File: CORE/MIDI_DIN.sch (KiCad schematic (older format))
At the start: 60 parts, among them J1 Conn_02x08_Odd_Even, J2 USB_C_Receptacle_USB2.0, J3 Conn_01x04, J5 MAB5100S, J6 MAB5100S, J7 Conn_01x06, Q1 BSS84, Q2 BSS84, SW1 SW_SPDT, SW2 SW_Push_DPDT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

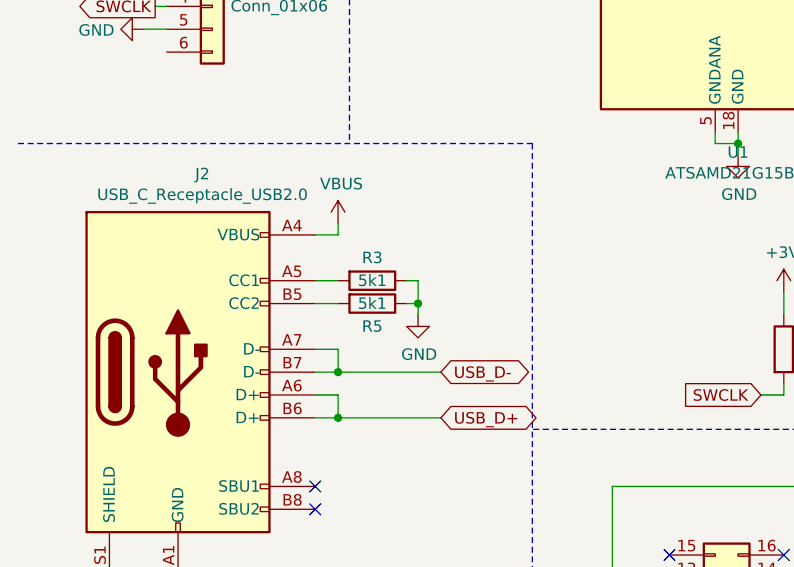
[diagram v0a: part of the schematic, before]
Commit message: Add pulldown for USB power protection
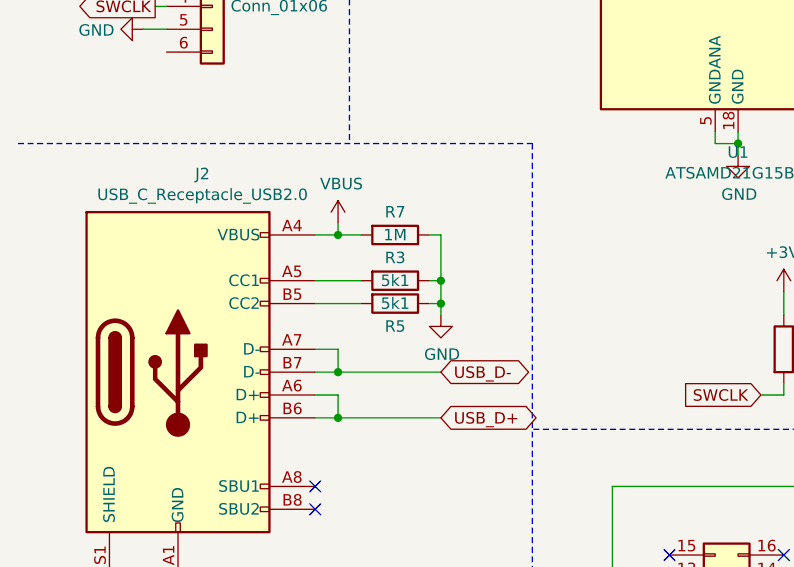
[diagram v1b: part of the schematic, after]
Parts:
- added R7: 1M, Resistor_SMD:R_0603_1608Metric, symbol Device:R
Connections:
- net GND: now also R7.1
- net VBUS: now also R7.2
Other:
- moved on the sheet: R3, R5
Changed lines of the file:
@@
 L Device:R R3
 U 1 1 60B7BED1
-P 2050 5600
-F 0 "R3" V 1950 5600 50  0000 C CNN
-F 1 "5k1" V 2050 5600 50  0000 C CNN
-F 2 "Resistor_SMD:R_0603_1608Metric" V 1980 5600 50  0001 C CNN
-F 3 "~" H 2050 5600 50  0001 C CNN
-	1    2050 5600
+P 2150 5600
+F 0 "R3" V 2050 5600 50  0000 C CNN
+F 1 "5k1" V 2150 5600 50  0000 C CNN
+F 2 "Resistor_SMD:R_0603_1608Metric" V 2080 5600 50  0001 C CNN
+F 3 "~" H 2150 5600 50  0001 C CNN
+	1    2150 5600
 	0    1    1    0
 $EndComp
@@
 L Device:R R5
 U 1 1 60B7CCB7
-P 2050 5700
-F 0 "R5" V 2150 5700 50  0000 C CNN
-F 1 "5k1" V 2050 5700 50  0000 C CNN
-F 2 "Resistor_SMD:R_0603_1608Metric" V 1980 5700 50  0001 C CNN
-F 3 "~" H 2050 5700 50  0001 C CNN
-	1    2050 5700
+P 2150 5700
+F 0 "R5" V 2250 5700 50  0000 C CNN
+F 1 "5k1" V 2150 5700 50  0000 C CNN
+F 2 "Resistor_SMD:R_0603_1608Metric" V 2080 5700 50  0001 C CNN
+F 3 "~" H 2150 5700 50  0001 C CNN
+	1    2150 5700
 	0    1    1    0
 $EndComp
@@
 L power:GND #PWR0125
 U 1 1 60B7D9BE
-P 2250 5750
-F 0 "#PWR0125" H 2250 5500 50  0001 C CNN
-F 1 "GND" H 2255 5577 50  0000 C CNN
-F 2 "" H 2250 5750 50  0001 C CNN
-F 3 "" H 2250 5750 50  0001 C CNN
-	1    2250 5750
-	1    0    0    -1
-$EndComp
-Wire Wire Line
-	2250 5750 2250 5700
-Wire Wire Line
-	2250 5700 2200 5700
-Wire Wire Line
-	2250 5700 2250 5600
-Wire Wire Line
-	2250 5600 2200 5600
-Connection ~ 2250 5700
-Wire Wire Line
-	1900 5600 1800 5600
-Wire Wire Line
-	1800 5700 1900 5700
+P 2350 5750
+F 0 "#PWR0125" H 2350 5500 50  0001 C CNN
+F 1 "GND" H 2355 5577 50  0000 C CNN
+F 2 "" H 2350 5750 50  0001 C CNN
+F 3 "" H 2350 5750 50  0001 C CNN
+	1    2350 5750
+	1    0    0    -1
+$EndComp
+Wire Wire Line
+	2350 5750 2350 5700
+Wire Wire Line
+	2350 5700 2300 5700
+Wire Wire Line
+	2350 5700 2350 5600
+Wire Wire Line
+	2350 5600 2300 5600
+Connection ~ 2350 5700
 $Comp
 L power:GND #PWR0126
@@
 Wire Wire Line
 	4350 6650 4350 6700
+$Comp
+L Device:R R7
+U 1 1 6418AC5D
+P 2150 5400
+F 0 "R7" V 2050 5400 50  0000 C CNN
+F 1 "1M" V 2150 5400 50  0000 C CNN
+F 2 "Resistor_SMD:R_0603_1608Metric" V 2080 5400 50  0001 C CNN
+F 3 "~" H 2150 5400 50  0001 C CNN
+	1    2150 5400
+	0    1    1    0
+$EndComp
+Wire Wire Line
+	1800 5700 2000 5700
+Wire Wire Line
+	1800 5600 2000 5600
+Wire Wire Line
+	1900 5400 2000 5400
+Connection ~ 1900 5400
+Wire Wire Line
+	2300 5400 2350 5400
+Wire Wire Line
+	2350 5400 2350 5600
+Connection ~ 2350 5600
 $EndSCHEMATC

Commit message: Rearrange and re-wire
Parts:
- removed Q2: BSS84, Package_TO_SOT_SMD:SOT-23, symbol Transistor_FET:BSS84
- removed R4: 10k, Resistor_SMD:R_0603_1608Metric, symbol Device:R
- added Q2, Q5: 2N7002, Package_TO_SOT_SMD:SOT-23, symbol Transistor_FET:2N7002
- added R24: 10k, Resistor_SMD:R_0603_1608Metric, symbol Device:R
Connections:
- net +5V: now also R9.1, R24.1
- net DIN_IN: now also R16.2, U2.4
- net DIN_OUT: now also Q2.1 (G)
- net GND: now also Q2.2 (S), Q5.2 (S); no longer R10.2
- net ActivityBUS renamed LED_IN
- net LED_IN: now also U1.30 (PA21); no longer U1.26 (PA17)
- net ActivityDIN renamed LED_OUT
- net LED_OUT: now also U1.26 (PA17); no longer U1.30 (PA21)
- net MIDIBUS+ renamed M2IDI+
- net MIDIBUS- renamed M2IDI-
- new net: Q5.3 (D), R10.2
- new net: Q2.3 (D), Q5.1 (G), R24.2
- no-connect marks 17 -> 18
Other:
- moved on the sheet: C12, C16, C3, D2, D3, D4, D5, D6, J3, J5, J6, J7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
